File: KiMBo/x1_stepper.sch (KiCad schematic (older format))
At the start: 25 parts, among them U28 TMC2130

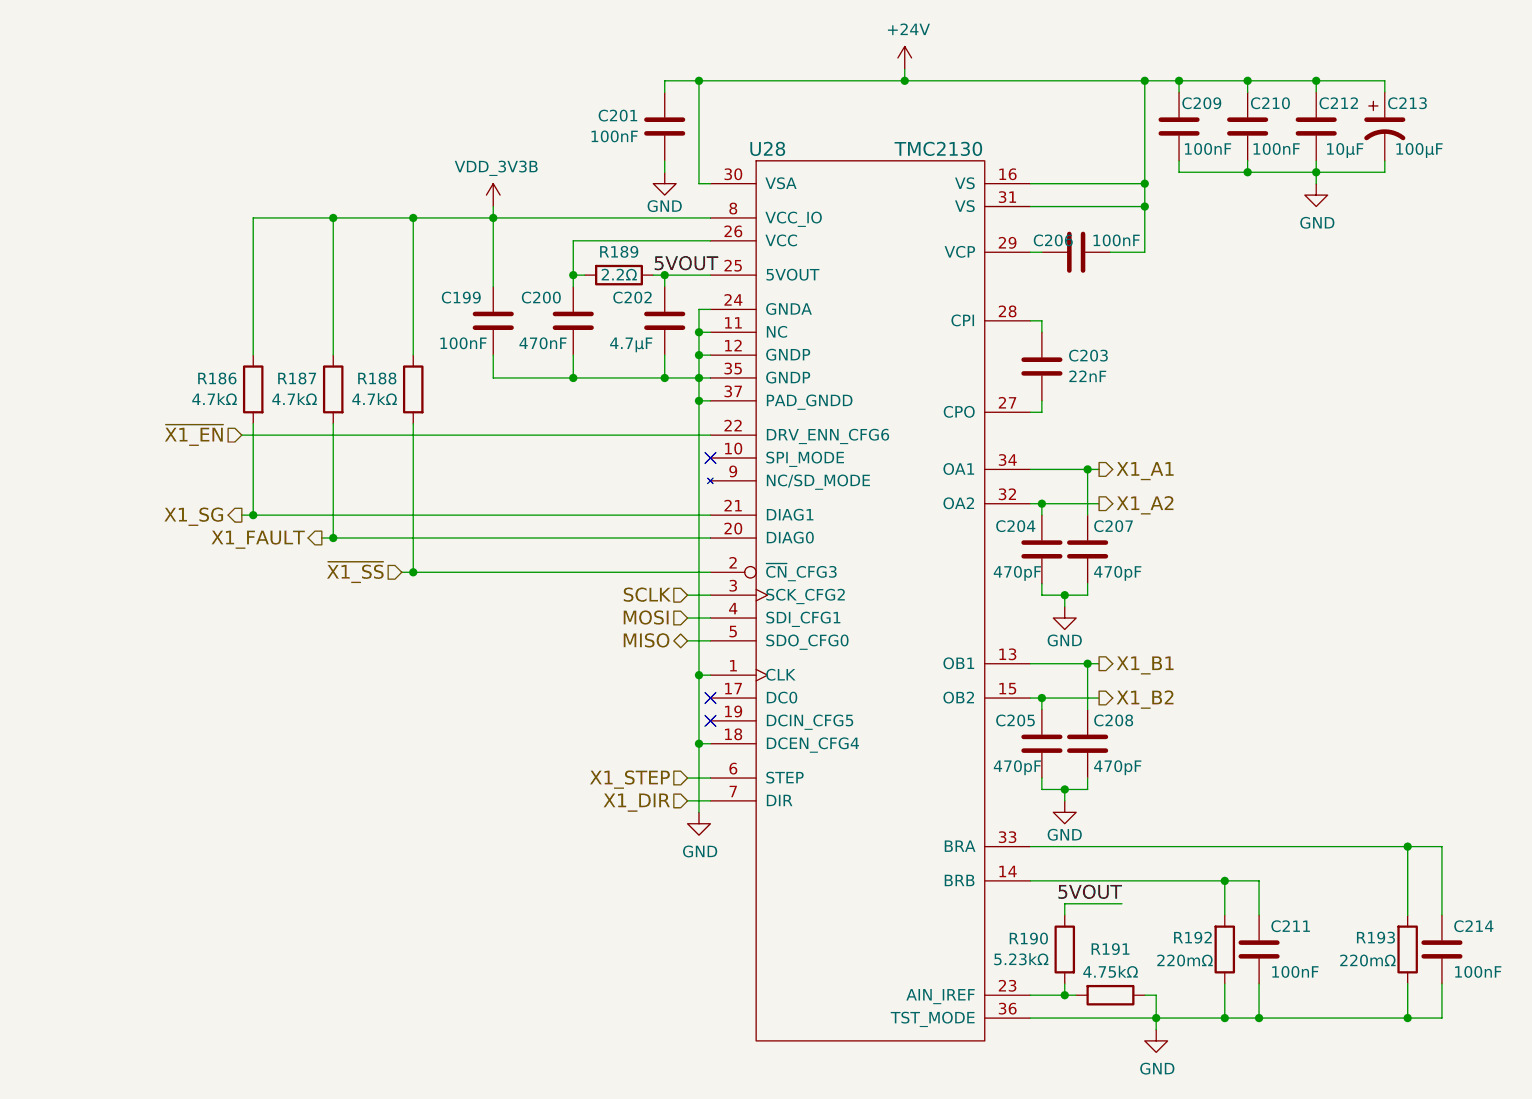
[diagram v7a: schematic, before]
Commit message: Connect X and Z stepper driver open-drain DIAG0 and DIAG1 lines together
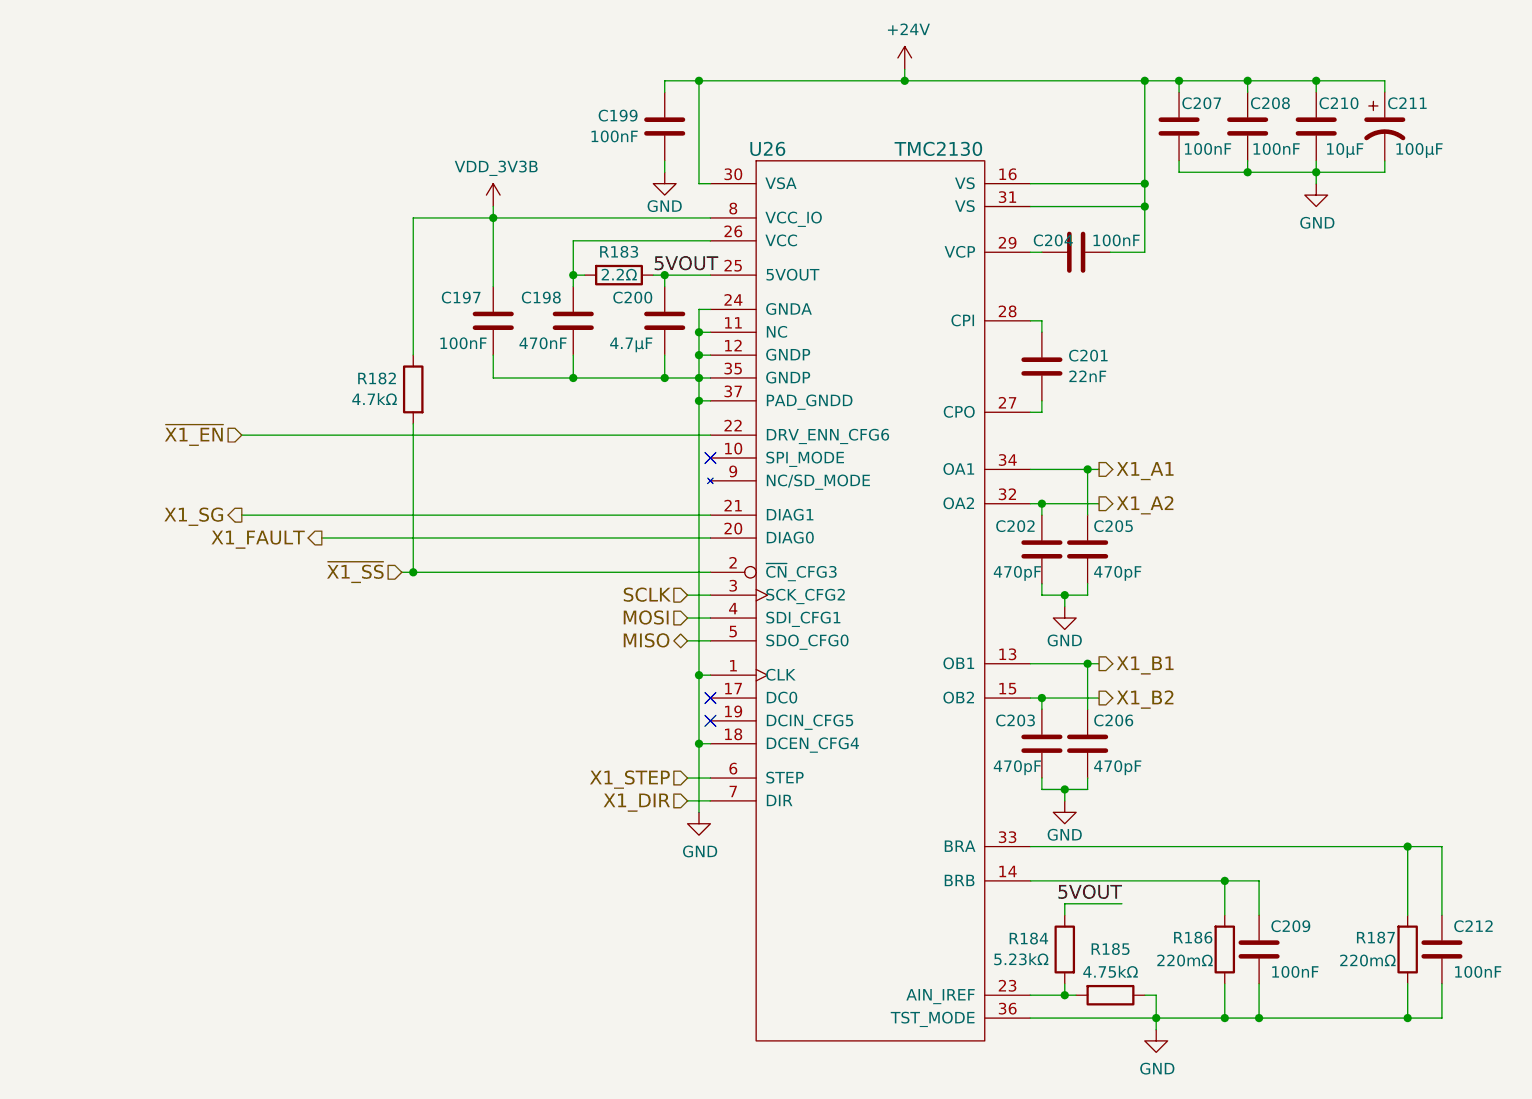
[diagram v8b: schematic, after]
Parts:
- removed R186, R187: 4.7kΩ, symbol R
- renumbered C199 to C197, C200 to C198, C201 to C199, C202 to C200, C203 to C201, C204 to C202, C205 to C203, C206 to C204, C207 to C205, C208 to C206, C209 to C207, C210 to C208, C211 to C209, C212 to C210, C213 to C211, C214 to C212, R188 to R182, R189 to R183, R190 to R184, R191 to R185, R192 to R186, R193 to R187, U28 to U26
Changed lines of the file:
@@
 X1_SG
 $Comp
-L C C201
+L C C199
 U 1 1 58C092B6
 P 7500 3100
-F 0 "C201" H 7386 3054 50  0000 R CNN
+F 0 "C199" H 7386 3054 50  0000 R CNN
 F 1 "100nF" H 7386 3145 50  0000 R CNN
 F 2 "Capacitors_SMD:C_0603" H 7538 2950 50  0001 C CNN
@@
 $EndComp
 $Comp
-L C C206
+L C C204
 U 1 1 58C092BD
 P 9300 3650
-F 0 "C206" V 9250 3550 50  0000 C CNN
+F 0 "C204" V 9250 3550 50  0000 C CNN
 F 1 "100nF" V 9250 3825 50  0000 C CNN
 F 2 "Capacitors_SMD:C_0603" H 9338 3500 50  0001 C CNN
@@
 $EndComp
 $Comp
-L CP1 C213
+L CP1 C211
 U 1 1 5BA7E13D
 P 10650 3100
-F 0 "C213" H 10750 3200 50  0000 C CNN
+F 0 "C211" H 10750 3200 50  0000 C CNN
 F 1 "100μF" H 10800 3000 50  0000 C CNN
 F 2 "Capacitors_SMD:c_elec_8x10" H 10650 3100 50  0001 C CNN
@@
 $EndComp
 $Comp
-L C C209
+L C C207
 U 1 1 5BA7E13E
 P 9750 3100
-F 0 "C209" H 9650 3200 50  0000 C CNN
+F 0 "C207" H 9650 3200 50  0000 C CNN
 F 1 "100nF" H 9625 3000 50  0000 C CNN
 F 2 "Capacitors_SMD:C_0603" H 9788 2950 50  0001 C CNN
@@
 $EndComp
 $Comp
-L GND #PWR0266
+L GND #PWR0256
 U 1 1 5BA7E13F
 P 7500 3300
-F 0 "#PWR0266" H 7500 3050 50  0001 C CNN
+F 0 "#PWR0256" H 7500 3050 50  0001 C CNN
 F 1 "GND" H 7500 3150 50  0000 C CNN
 F 2 "" H 7500 3300 50  0000 C CNN
@@
 $EndComp
 $Comp
-L C C210
+L C C208
 U 1 1 58C092D8
 P 10050 3100
-F 0 "C210" H 9950 3200 50  0000 C CNN
+F 0 "C208" H 9950 3200 50  0000 C CNN
 F 1 "100nF" H 9925 3000 50  0000 C CNN
 F 2 "Capacitors_SMD:C_0603" H 10088 2950 50  0001 C CNN
@@
 $EndComp
 $Comp
-L GND #PWR0267
+L GND #PWR0257
 U 1 1 58C092DF
 P 10350 3350
-F 0 "#PWR0267" H 10350 3100 50  0001 C CNN
+F 0 "#PWR0257" H 10350 3100 50  0001 C CNN
 F 1 "GND" H 10355 3177 50  0000 C CNN
 F 2 "" H 10350 3350 50  0000 C CNN
@@
 $EndComp
 $Comp
-L +24V #PWR0268
+L +24V #PWR0258
 U 1 1 5BA7E142
 P 8550 2850
-F 0 "#PWR0268" H 8550 2700 50  0001 C CNN
+F 0 "#PWR0258" H 8550 2700 50  0001 C CNN
 F 1 "+24V" H 8565 3023 50  0000 C CNN
 F 2 "" H 8550 2850 50  0000 C CNN
@@
 $EndComp
 $Comp
-L C C203
+L C C201
 U 1 1 5BA7E143
 P 9150 4150
-F 0 "C203" H 9265 4196 50  0000 L CNN
+F 0 "C201" H 9265 4196 50  0000 L CNN
 F 1 "22nF" H 9265 4105 50  0000 L CNN
 F 2 "Capacitors_SMD:C_0402" H 9188 4000 50  0001 C CNN
@@
 $EndComp
 $Comp
-L R R193
+L R R187
 U 1 1 5BA7E144
 P 10750 6700
-F 0 "R193" H 10700 6650 50  0000 R CNN
+F 0 "R187" H 10700 6650 50  0000 R CNN
 F 1 "220mΩ" H 10700 6750 50  0000 R CNN
 F 2 "" V 10680 6700 50  0001 C CNN
@@
 $EndComp
 $Comp
-L R R192
+L R R186
 U 1 1 5BA7E145
 P 9950 6700
-F 0 "R192" H 9900 6650 50  0000 R CNN
+F 0 "R186" H 9900 6650 50  0000 R CNN
 F 1 "220mΩ" H 9900 6750 50  0000 R CNN
 F 2 "" V 9880 6700 50  0001 C CNN
@@
 $EndComp
 $Comp
-L GND #PWR0269
+L GND #PWR0259
 U 1 1 58C09300
 P 9650 7050
-F 0 "#PWR0269" H 9650 6800 50  0001 C CNN
+F 0 "#PWR0259" H 9650 6800 50  0001 C CNN
 F 1 "GND" H 9655 6877 50  0000 C CNN
 F 2 "" H 9650 7050 50  0000 C CNN
@@
 NoConn ~ 7700 5600
 $Comp
-L R R189
+L R R183
 U 1 1 58C09307
 P 7300 3750
-F 0 "R189" V 7200 3750 50  0000 C CNN
+F 0 "R183" V 7200 3750 50  0000 C CNN
 F 1 "2.2Ω" V 7300 3750 50  0000 C CNN
 F 2 "" V 7230 3750 50  0001 C CNN
@@
 $EndComp
 $Comp
-L C C200
+L C C198
 U 1 1 58C0930E
 P 7100 3950
-F 0 "C200" H 7150 4050 50  0000 L CNN
+F 0 "C198" H 7150 4050 50  0000 L CNN
 F 1 "470nF" H 7125 3850 50  0000 L CNN
 F 2 "Capacitors_SMD:C_0603" H 7138 3800 50  0001 C CNN
@@
 NoConn ~ 7700 5700
 $Comp
-L GND #PWR0270
+L GND #PWR0260
 U 1 1 58C09323
 P 7650 6100
-F 0 "#PWR0270" H 7650 5850 50  0001 C CNN
+F 0 "#PWR0260" H 7650 5850 50  0001 C CNN
 F 1 "GND" H 7655 5927 50  0000 C CNN
 F 2 "" H 7650 6100 50  0000 C CNN
@@
 $EndComp
 $Comp
-L C C211
+L C C209
 U 1 1 58C09329
 P 10100 6700
-F 0 "C211" H 10150 6800 50  0000 L CNN
+F 0 "C209" H 10150 6800 50  0000 L CNN
 F 1 "100nF" H 10150 6600 50  0000 L CNN
 F 2 "Capacitors_SMD:C_0603" H 10138 6550 50  0001 C CNN
@@
 Text HLabel 6000 4900 0    60   Output ~ 0
 X1_FAULT
-$Comp
-L R R187
-U 1 1 5BA7E14B
-P 6050 4250
-F 0 "R187" H 6119 4296 50  0000 L CNN
-F 1 "4.7kΩ" H 6119 4205 50  0000 L CNN
-F 2 "" V 5980 4250 50  0001 C CNN
-F 3 "" H 6050 4250 50  0000 C CNN
-	1    6050 4250
-	-1   0    0    -1
-$EndComp
 Text HLabel 5650 4450 0    60   Input ~ 0
 ~X1_EN
 NoConn ~ 7700 4550
 $Comp
-L C C202
+L C C200
 U 1 1 58C0933B
 P 7500 3950
-F 0 "C202" H 7550 4050 50  0000 L CNN
+F 0 "C200" H 7550 4050 50  0000 L CNN
 F 1 "4.7μF" H 7550 3850 50  0000 L CNN
 F 2 "Capacitors_SMD:C_0402" H 7538 3800 50  0001 C CNN
@@
 5VOUT
 $Comp
-L R R190
+L R R184
 U 1 1 58C09343
 P 9250 6700
-F 0 "R190" H 9319 6746 50  0000 L CNN
+F 0 "R184" H 9319 6746 50  0000 L CNN
 F 1 "5.23kΩ" H 9319 6655 50  0000 L CNN
 F 2 "" V 9180 6700 50  0001 C CNN
@@
 5VOUT
 $Comp
-L R R191
+L R R185
 U 1 1 58C0934B
 P 9450 6900
-F 0 "R191" V 9250 6900 50  0000 C CNN
+F 0 "R185" V 9250 6900 50  0000 C CNN
 F 1 "4.75kΩ" V 9350 6900 50  0000 C CNN
 F 2 "" V 9380 6900 50  0001 C CNN
@@
 $EndComp
 $Comp
-L R R188
+L R R182
 U 1 1 5BA7E14F
 P 6400 4250
-F 0 "R188" H 6469 4296 50  0000 L CNN
+F 0 "R182" H 6469 4296 50  0000 L CNN
 F 1 "4.7kΩ" H 6469 4205 50  0000 L CNN
 F 2 "" V 6330 4250 50  0001 C CNN
@@
 $EndComp
 $Comp
-L C C214
+L C C212
 U 1 1 5BA7E150
 P 10900 6700
-F 0 "C214" H 10950 6800 50  0000 L CNN
+F 0 "C212" H 10950 6800 50  0000 L CNN
 F 1 "100nF" H 10950 6600 50  0000 L CNN
 F 2 "Capacitors_SMD:C_0603" H 10938 6550 50  0001 C CNN
@@
 $EndComp
 $Comp
-L C C204
+L C C202
 U 1 1 5BA7E151
 P 9150 4950
-F 0 "C204" H 9175 5050 50  0000 L CNN
+F 0 "C202" H 9175 5050 50  0000 L CNN
 F 1 "470pF" H 9150 4850 50  0000 L CNN
 F 2 "Capacitors_SMD:C_0603" H 9188 4800 50  0001 C CNN
@@
 $EndComp
 $Comp
-L GND #PWR0271
+L GND #PWR0261
 U 1 1 5BA7E152
 P 9250 5200
-F 0 "#PWR0271" H 9250 4950 50  0001 C CNN
+F 0 "#PWR0261" H 9250 4950 50  0001 C CNN
 F 1 "GND" H 9250 5050 50  0000 C CNN
 F 2 "" H 9250 5200 50  0000 C CNN
@@
 $EndComp
 $Comp
-L C C207
+L C C205
 U 1 1 5BA7E153
 P 9350 4950
-F 0 "C207" H 9375 5050 50  0000 L CNN
+F 0 "C205" H 9375 5050 50  0000 L CNN
 F 1 "470pF" H 9375 4850 50  0000 L CNN
 F 2 "Capacitors_SMD:C_0603" H 9388 4800 50  0001 C CNN
@@
 $EndComp
 $Comp
-L C C205
+L C C203
 U 1 1 58C09377
 P 9150 5800
-F 0 "C205" H 9175 5900 50  0000 L CNN
+F 0 "C203" H 9175 5900 50  0000 L CNN
 F 1 "470pF" H 9150 5700 50  0000 L CNN
 F 2 "Capacitors_SMD:C_0603" H 9188 5650 50  0001 C CNN
@@
 $EndComp
 $Comp
-L GND #PWR0272
+L GND #PWR0262
 U 1 1 5BA7E155
 P 9250 6050
-F 0 "#PWR0272" H 9250 5800 50  0001 C CNN
+F 0 "#PWR0262" H 9250 5800 50  0001 C CNN
 F 1 "GND" H 9250 5900 50  0000 C CNN
 F 2 "" H 9250 6050 50  0000 C CNN
@@
 $EndComp
 $Comp
-L C C208
+L C C206
 U 1 1 5BA7E156
 P 9350 5800
-F 0 "C208" H 9375 5900 50  0000 L CNN
+F 0 "C206" H 9375 5900 50  0000 L CNN
 F 1 "470pF" H 9375 5700 50  0000 L CNN
 F 2 "Capacitors_SMD:C_0603" H 9388 5650 50  0001 C CNN
@@
 $EndComp
 $Comp
-L TMC2130 U28
+L TMC2130 U26
 U 1 1 5BA7E157
 P 8400 4700
-F 0 "U28" H 7950 6200 60  0000 C CNN
+F 0 "U26" H 7950 6200 60  0000 C CNN
 F 1 "TMC2130" H 8700 6200 60  0000 C CNN
 F 2 "" H 8400 5000 60  0001 C CNN
@@
 	6000 4900 7700 4900
 Wire Wire Line
-	6050 4400 6050 4900
-Wire Wire Line
-	6050 4100 6050 3500
-Connection ~ 6050 4900
-Wire Wire Line
 	5650 4450 7700 4450
 Wire Wire Line
@@
 Wire Wire Line
 	6400 3500 6400 4100
-Connection ~ 6400 3500
 Wire Wire Line
 	5650 4800 7700 4800
@@
 	9150 6000 9150 5950
 $Comp
-L R R186
-U 1 1 58C093FF
-P 5700 4250
-F 0 "R186" H 5769 4296 50  0000 L CNN
-F 1 "4.7kΩ" H 5769 4205 50  0000 L CNN
-F 2 "" V 5630 4250 50  0001 C CNN
-F 3 "" H 5700 4250 50  0000 C CNN
-	1    5700 4250
-	-1   0    0    -1
-$EndComp
-Wire Wire Line
-	5700 4400 5700 4800
-Connection ~ 5700 4800
-Wire Wire Line
-	5700 4100 5700 3500
-Connection ~ 6050 3500
-$Comp
-L C C212
+L C C210
 U 1 1 58C0940A
 P 10350 3100
-F 0 "C212" H 10250 3200 50  0000 C CNN
+F 0 "C210" H 10250 3200 50  0000 C CNN
 F 1 "10μF" H 10225 3000 50  0000 C CNN
 F 2 "Capacitors_SMD:C_0805" H 10388 2950 50  0001 C CNN
@@
 	9100 4600 9400 4600
 Wire Wire Line
-	5700 3500 7700 3500
-$Comp
-L VDD_3V3B #PWR0273
+	6400 3500 7700 3500
+$Comp
+L VDD_3V3B #PWR0263
 U 1 1 5BA7E15A
 P 6750 3450
-F 0 "#PWR0273" H 6750 3300 50  0001 C CNN
+F 0 "#PWR0263" H 6750 3300 50  0001 C CNN
 F 1 "VDD_3V3B" H 6765 3623 50  0000 C CNN
 F 2 "" H 6750 3450 50  0000 C CNN
@@
 $EndComp
 $Comp
-L C C199
+L C C197
 U 1 1 5A89A0A1
 P 6750 3950
-F 0 "C199" H 6800 4050 50  0000 L CNN
+F 0 "C197" H 6800 4050 50  0000 L CNN
 F 1 "100nF" H 6775 3850 50  0000 L CNN
 F 2 "Capacitors_SMD:C_0603" H 6788 3800 50  0001 C CNN
